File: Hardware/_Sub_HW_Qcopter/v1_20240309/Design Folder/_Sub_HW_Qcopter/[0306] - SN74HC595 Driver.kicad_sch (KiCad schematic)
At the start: 0 parts

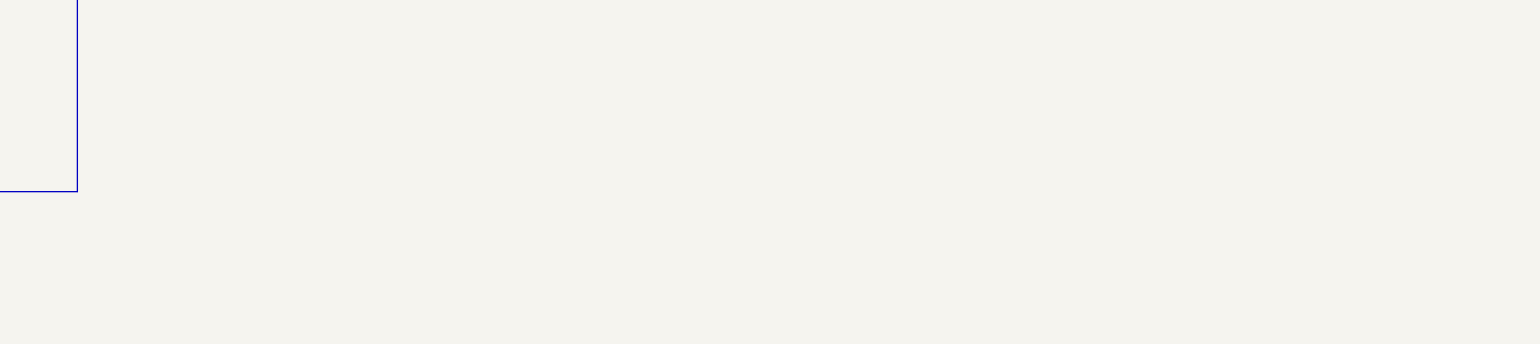
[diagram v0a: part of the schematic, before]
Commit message: Schematic is done by 90%
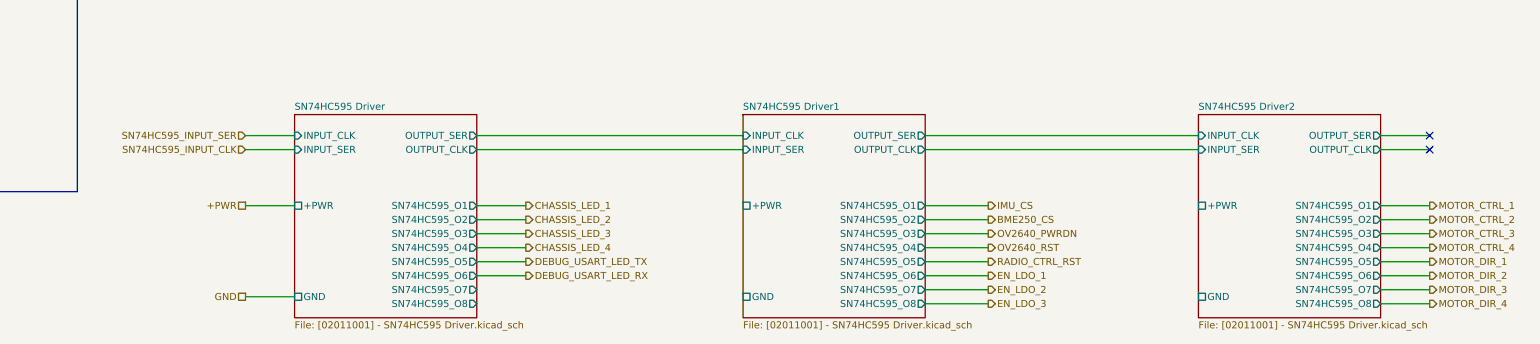
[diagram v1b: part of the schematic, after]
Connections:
- no-connect marks 0 -> 2
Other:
- added sheet SN74HC595 Driver ([02011001] - SN74HC595 Driver.kicad_sch)
- added sheet SN74HC595 Driver1 ([02011001] - SN74HC595 Driver.kicad_sch)
- added sheet SN74HC595 Driver2 ([02011001] - SN74HC595 Driver.kicad_sch)
